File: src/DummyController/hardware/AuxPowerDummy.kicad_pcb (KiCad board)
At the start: 2 copper layers, 90 x 90 mm, 58 parts, among them J1 MC 1,5/2, J10 MC 1,5/4, J11 S3B-XH-A, J12 S3B-XH-A, J13 S3B-XH-A, J14 S3B-XH-A, J15 S3B-XH-A, J16 B3B-XH-A, J17 B4B-XH-A, J2 MC 1,5/2, J3 MC 1,5/2, J4 MC 1,5/2, J5 MC 1,5/2, J6 MC 1,5/4, J7 MC 1,5/4, J8 MC 1,5/4, J9 MC 1,5/4, Q1 BC846B,235, Q2 BC846B,235, Q3 BC846B,235, Q4 BC846B,235, Q5 BC846B,235

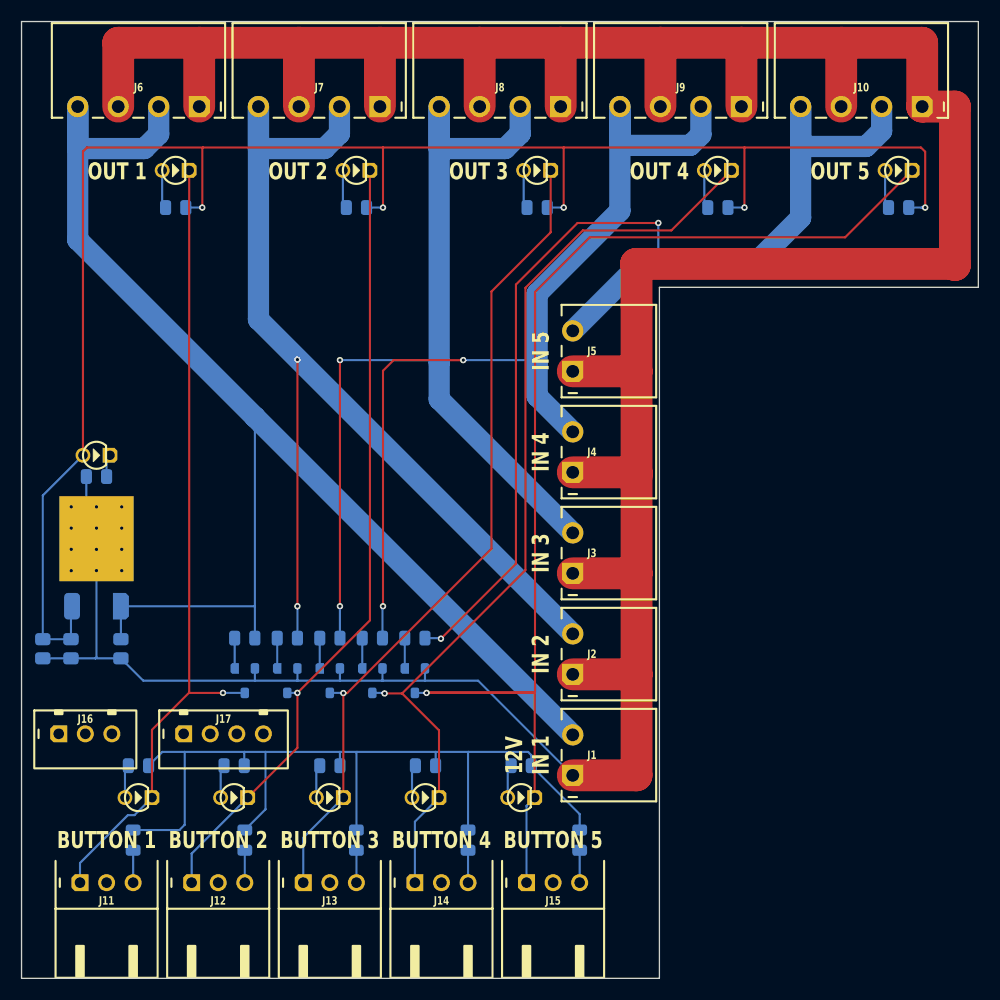
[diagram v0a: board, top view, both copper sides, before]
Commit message: Increased trace width for power
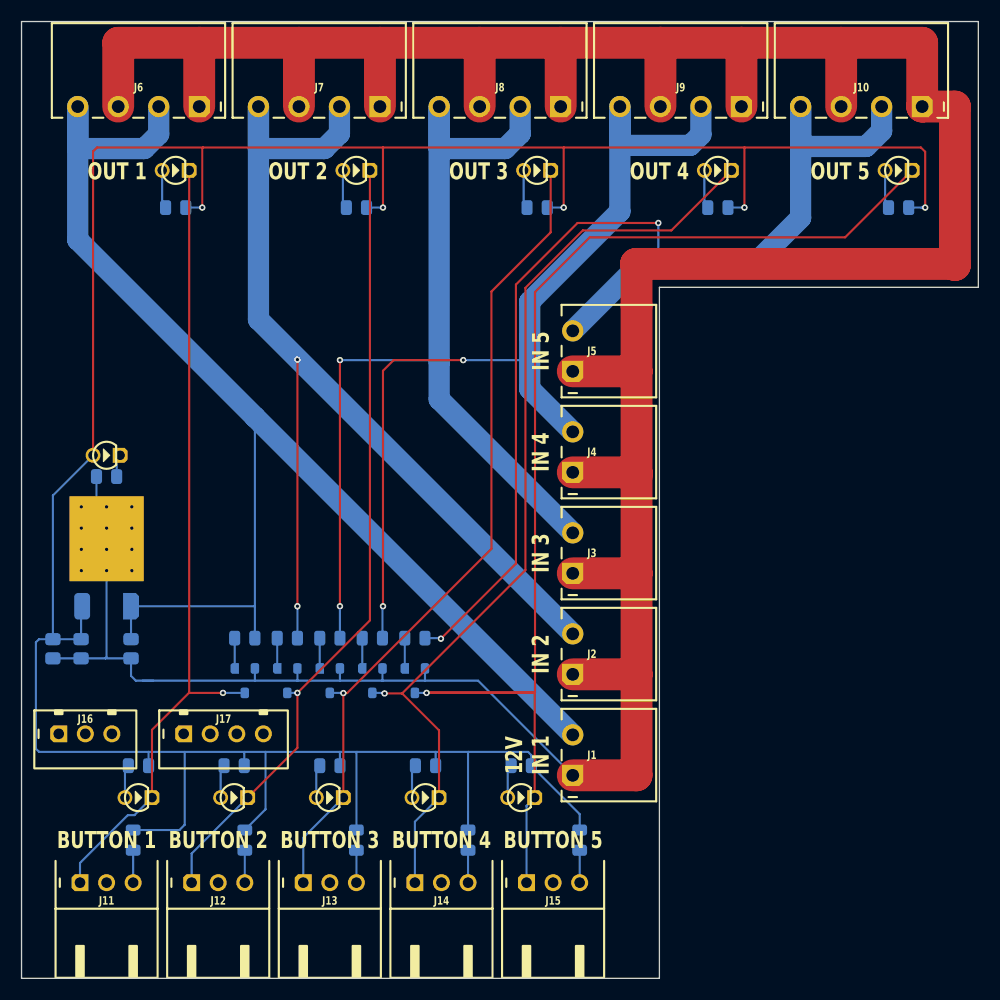
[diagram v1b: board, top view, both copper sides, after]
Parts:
- moved C1 0.95 mm to (20.6, 74.0)
- moved C2 0.95 mm to (25.3, 74.0)
- moved C3 0.95 mm to (17.9, 74.0)
- moved DS11 0.95 mm to (23.0, 55.8)
- moved R16 0.95 mm to (23.0, 57.8)
- moved VR1 0.95 mm to (23.0, 70.0)
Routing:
- net 5V: track 252.6 -> 274.8 mm
- net INPUT4: track 89.7 -> 91.8 mm
- net GND: track 360.9 -> 361.9 mm
- net INPUT1: track 129.6 -> 128.6 mm
